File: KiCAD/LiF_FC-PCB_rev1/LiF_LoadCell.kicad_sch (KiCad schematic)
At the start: 29 parts, among them J17 LC 5V0_{EN}, J18 LC 3V3_{EN}, J19 Load Cell, U8 MCP6N11-xxxE/SN, U9 NCV8114ASN165T1G

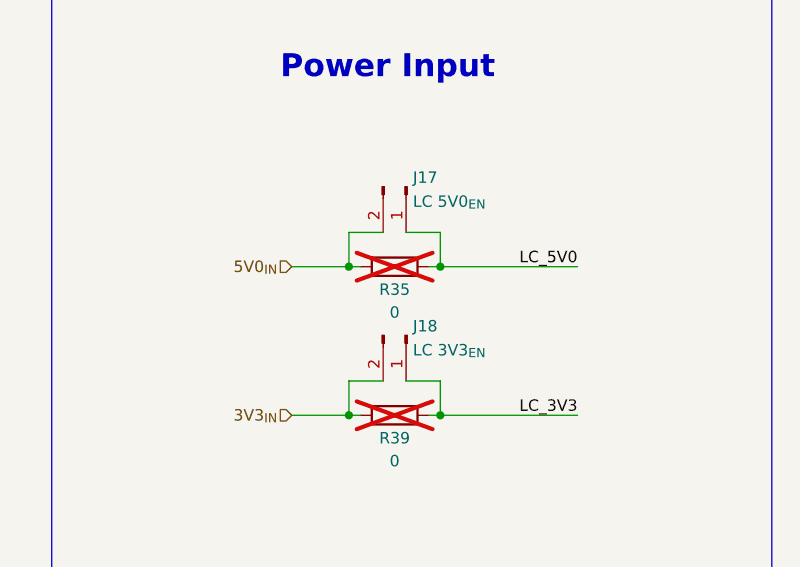
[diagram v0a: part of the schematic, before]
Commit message: Created new KiCAD project for IO PCB, moved relevant components there, saving backup before reannotating the Service PCB schematics
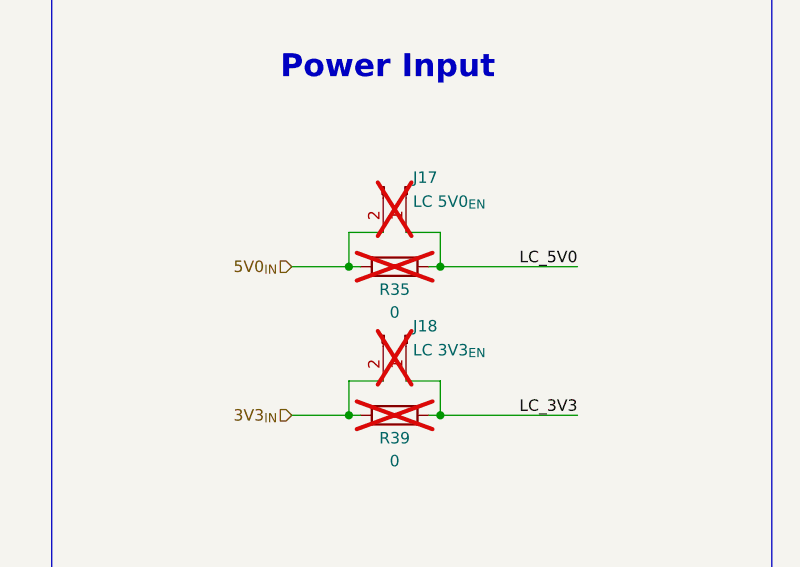
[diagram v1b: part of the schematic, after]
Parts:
- J17, J18: now not fitted; now left out of the parts list

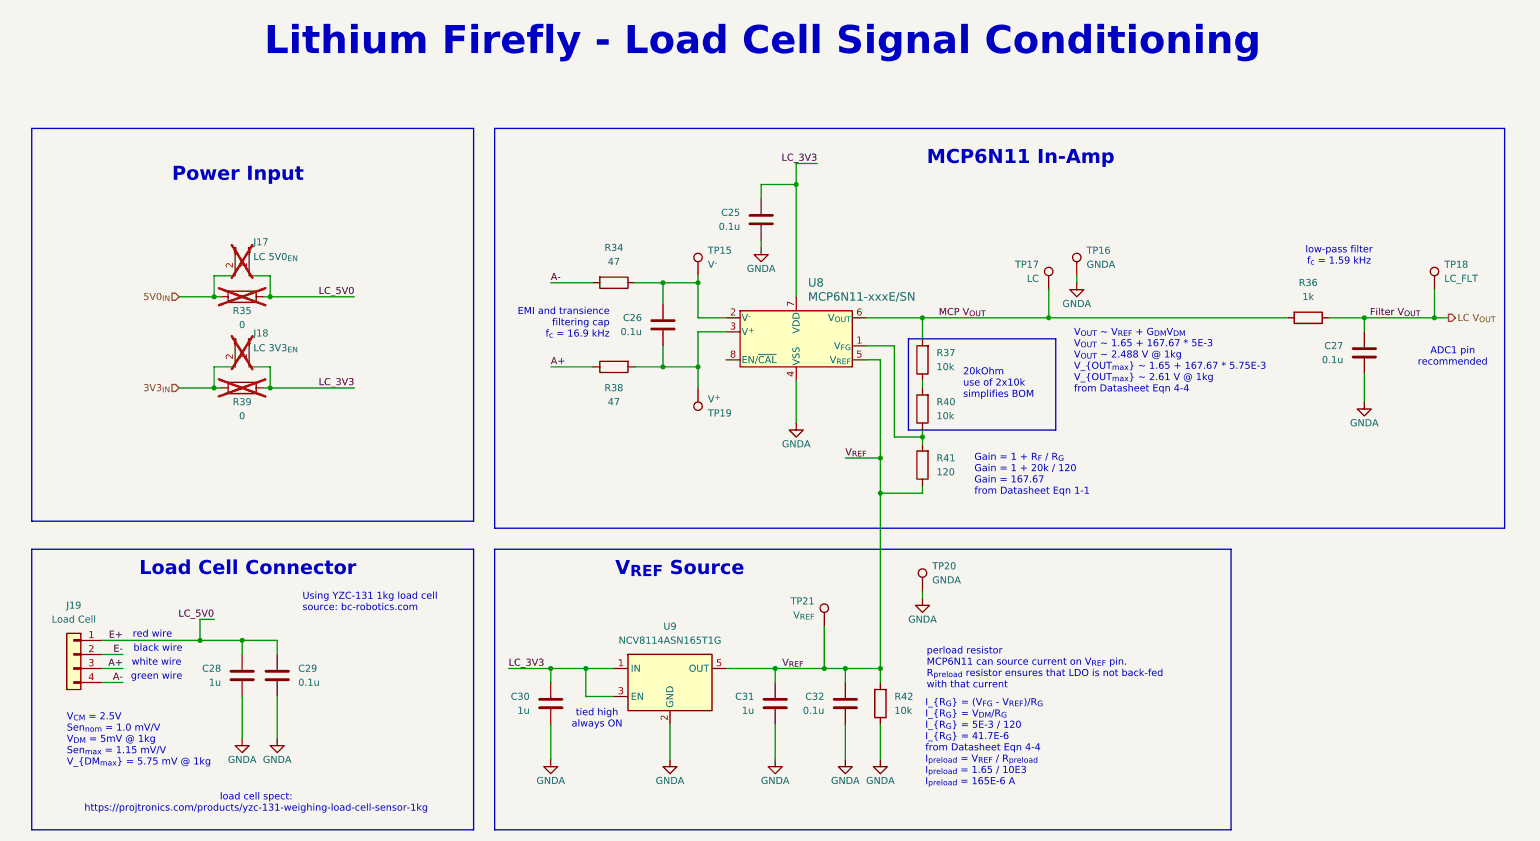
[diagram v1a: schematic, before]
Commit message: progress save for the night. landmarking of service PCB is almost done. redid the analog section layout to make it more assembleable and better utilze the space. Still need to do ACC, R3V3, IO, test points, and jumpers
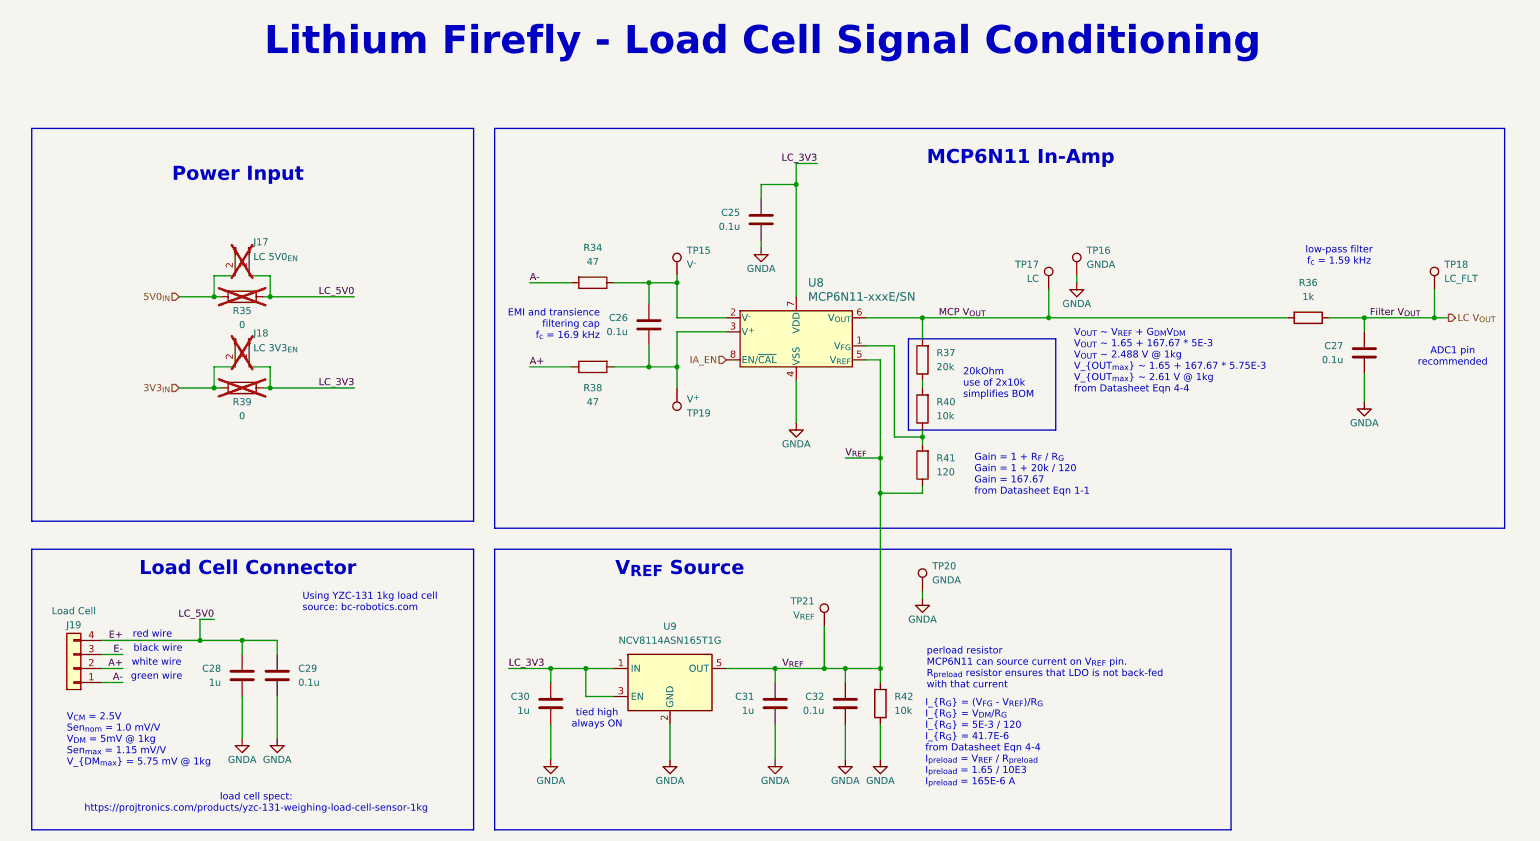
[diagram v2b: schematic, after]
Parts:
- R37: value 10k -> 20k
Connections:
- net A+: now also J19.2 (Pin_2); no longer J19.3 (Pin_3)
- net A-: now also J19.1 (Pin_1); no longer J19.4 (Pin_4)
- net E+: now also J19.4 (Pin_4); no longer J19.1 (Pin_1)
- net E-: now also J19.3 (Pin_3); no longer J19.2 (Pin_2)
- net IA_EN: now reaches U8.8 (EN/~{CAL})
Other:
- moved on the sheet: C26, J19, R34, R38, TP15, TP19

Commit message: routing backup
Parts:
- R39: now left out of the parts list
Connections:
- net LC_3V3 is gone; now on net 3V3_{IN}: C25.1, C30.1, J18.1 (Pin_1), R39.1, U8.7 (VDD), U9.1 (IN), U9.3 (EN)
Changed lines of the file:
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@@
+	)
+	(junction
+		(at 62.23 82.55)
+		(diameter 0)
+		(color 0 0 0 0)
 	)
 	(junction
@@
 	)
 	(junction
+		(at 44.45 82.55)
+		(diameter 0)
+		(color 0 0 0 0)
+	)
+	(junction
 		(at 132.08 78.74)
 		(diameter 0)
@@
 	(wire
 		(pts
+			(xy 62.23 82.55) (xy 73.66 82.55)
+		)
+		(stroke
+			(width 0)
+			(type default)
+		)
+	)
+	(wire
+		(pts
 			(xy 127 78.74) (xy 132.08 78.74)
 		)
@@
 	(wire
 		(pts
-			(xy 41.91 82.55) (xy 48.26 82.55)
+			(xy 41.91 82.55) (xy 44.45 82.55)
 		)
 		(stroke
@@
 	(wire
 		(pts
+			(xy 44.45 90.17) (xy 44.45 82.55)
+		)
+		(stroke
+			(width 0)
+			(type default)
+		)
+	)
+	(wire
+		(pts
 			(xy 45.72 124.46) (xy 45.72 128.27)
 		)
@@
 	(wire
 		(pts
+			(xy 44.45 82.55) (xy 48.26 82.55)
+		)
+		(stroke
+			(width 0)
+			(type default)
+		)
+	)
+	(wire
+		(pts
 			(xy 162.56 133.35) (xy 168.91 133.35)
 		)
@@
 	(wire
 		(pts
-			(xy 58.42 82.55) (xy 73.66 82.55)
+			(xy 58.42 82.55) (xy 62.23 82.55)
 		)
 		(stroke
@@
 	(wire
 		(pts
+			(xy 62.23 90.17) (xy 44.45 90.17)
+		)
+		(stroke
+			(width 0)
+			(type default)
+		)
+	)
+	(wire
+		(pts
 			(xy 120.65 63.5) (xy 127 63.5)
 		)
@@
 		(pts
 			(xy 256.54 80.01) (xy 256.54 85.09)
+		)
+		(stroke
+			(width 0)
+			(type default)
+		)
+	)
+	(wire
+		(pts
+			(xy 62.23 82.55) (xy 62.23 90.17)
 		)
 		(stroke
@@
 		(unit 1)
 		(exclude_from_sim no)
-		(in_bom yes)
-		(on_board yes)
+		(in_bom no)
+		(on_board no)
 		(dnp yes)
 		(property "Reference" "R39"

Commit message: finished service PCB routing and silkscreen, finished IO PCB layout, routing, and silkscreen. Exported production files, submitted PCB for manufacturing by JLCPCB
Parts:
- removed TP20: GNDA, TestPoint:TestPoint_Loop_D1.80mm_Drill1.0mm_Beaded, symbol Connector:TestPoint
- R34, R36, R37, R38, R40, R41, R42: footprint Capacitor_SMD:C_0805_2012Metric -> Resistor_SMD:R_0805_2012Metric
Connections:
- net E- is gone; now on net GNDA: J19.3 (Pin_3)
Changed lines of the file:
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@@
 	(wire
 		(pts
-			(xy 27.94 130.81) (xy 31.75 130.81)
+			(xy 27.94 130.81) (xy 44.45 130.81)
 		)
 		(stroke
@@
 	(wire
 		(pts
-			(xy 176.53 119.38) (xy 176.53 120.65)
+			(xy 44.45 139.7) (xy 44.45 130.81)
 		)
 		(stroke
@@
 	)
 	(symbol
-		(lib_id "power:GNDA")
-		(at 176.53 120.65 0)
+		(lib_id "Connector:TestPoint")
+		(at 269.24 64.77 0)
 		(unit 1)
 		(exclude_from_sim no)
@@
 		(on_board yes)
 		(dnp no)
-		(property "Reference" "#PWR051"
-			(at 176.53 127 0)
+		(property "Reference" "TP18"
+			(at 271.018 60.198 0)
 			(effects
 				(font
 					(size 1.27 1.27)
 				)
-				(hide yes)
+				(justify left)
 			)
 		)
-		(property "Value" "GNDA"
-			(at 176.53 124.46 0)
+		(property "Value" "LC_FLT"
+			(at 271.018 62.738 0)
 			(effects
 				(font
 					(size 1.27 1.27)
 				)
+				(justify left)
 			)
 		)
-		(property "Footprint" ""
-			(at 176.53 120.65 0)
+		(property "Footprint" "TestPoint:TestPoint_Loop_D1.80mm_Drill1.0mm_Beaded"
+			(at 274.32 64.77 0)
 			(effects
 				(font
@@
 			)
 		)
-		(property "Datasheet" ""
-			(at 176.53 120.65 0)
+		(property "Datasheet" "~"
+			(at 274.32 64.77 0)
 			(effects
 				(font
@@
 			)
 		)
-		(property "Description" ""
-			(at 176.53 120.65 0)
+		(property "Description" "test point"
+			(at 269.24 64.77 0)
 			(effects
 				(font
@@
 			)
 		)
-		(pin "1"
-		)
-		(instances
-			(project "LiF_FC-PCB_rev1"
-				(path "/9e3e8da7-e506-46c9-90e5-307e4ad30d29/17577359-df8d-4d28-9071-787d31b1b6da"
-					(reference "#PWR051")
-					(unit 1)
-				)
-			)
-		)
-	)
-	(symbol
-		(lib_id "Connector:TestPoint")
-		(at 269.24 64.77 0)
-		(unit 1)
-		(exclude_from_sim no)
-		(in_bom yes)
-		(on_board yes)
-		(dnp no)
-		(property "Reference" "TP18"
-			(at 271.018 60.198 0)
+		(property "PN" "5002"
+			(at 269.24 64.77 0)
 			(effects
 				(font
 					(size 1.27 1.27)
 				)
-				(justify left)
+				(hide yes)
 			)
 		)
-		(property "Value" "LC_FLT"
-			(at 271.018 62.738 0)
+		(property "DKPN" "36-5002-ND"
+			(at 269.24 64.77 0)
 			(effects
 				(font
 					(size 1.27 1.27)
 				)
-				(justify left)
+				(hide yes)
 			)
 		)
-		(property "Footprint" "TestPoint:TestPoint_Loop_D1.80mm_Drill1.0mm_Beaded"
-			(at 274.32 64.77 0)
+		(property "CREATOR" ""
+			(at 269.24 64.77 0)
 			(effects
 				(font
@@
 			)
 		)
-		(property "Datasheet" "~"
-			(at 274.32 64.77 0)
+		(property "Check_prices" ""
+			(at 269.24 64.77 0)
 			(effects
 				(font
@@
 			)
 		)
-		(property "Description" "test point"
+		(property "Description_1" ""
 			(at 269.24 64.77 0)
 			(effects
@@
 			)
 		)
-		(property "PN" "5002"
+		(property "DigiKey_Part_Number" ""
 			(at 269.24 64.77 0)
 			(effects
@@
 			)
 		)
-		(property "DKPN" "36-5002-ND"
+		(property "Package" ""
 			(at 269.24 64.77 0)
 			(effects
@@
 			)
 		)
-		(property "CREATOR" ""
+		(property "SNAPEDA_PN" ""
 			(at 269.24 64.77 0)
 			(effects
@@
 			)
 		)
-		(property "Check_prices" ""
+		(property "SnapEDA_Link" ""
 			(at 269.24 64.77 0)
 			(effects
@@
 			)
 		)
-		(property "Description_1" ""
+		(property "VERIFIER" ""
 			(at 269.24 64.77 0)
 			(effects
@@
 			)
 		)
-		(property "DigiKey_Part_Number" ""
-			(at 269.24 64.77 0)
+		(pin "1"
+		)
+		(instances
+			(project "LiF_FC-PCB_rev1"
+				(path "/9e3e8da7-e506-46c9-90e5-307e4ad30d29/17577359-df8d-4d28-9071-787d31b1b6da"
+					(reference "TP18")
+					(unit 1)
+				)
+			)
+		)
+	)
+	(symbol
+		(lib_id "power:GNDA")
+		(at 44.45 139.7 0)
+		(unit 1)
+		(exclude_from_sim no)
+		(in_bom yes)
+		(on_board yes)
+		(dnp no)
+		(property "Reference" "#PWR02"
+			(at 44.45 146.05 0)
 			(effects
 				(font
@@
 			)
 		)
-		(property "Package" ""
-			(at 269.24 64.77 0)
+		(property "Value" "GNDA"
+			(at 44.45 143.51 0)
 			(effects
 				(font
 					(size 1.27 1.27)
 				)
-				(hide yes)
 			)
 		)
-		(property "SNAPEDA_PN" ""
-			(at 269.24 64.77 0)
+		(property "Footprint" ""
+			(at 44.45 139.7 0)
 			(effects
 				(font
@@
 			)
 		)
-		(property "SnapEDA_Link" ""
-			(at 269.24 64.77 0)
+		(property "Datasheet" ""
+			(at 44.45 139.7 0)
 			(effects
 				(font
@@
 			)
 		)
-		(property "VERIFIER" ""
-			(at 269.24 64.77 0)
+		(property "Description" ""
+			(at 44.45 139.7 0)
 			(effects
 				(font
@@
 			(project "LiF_FC-PCB_rev1"
 				(path "/9e3e8da7-e506-46c9-90e5-307e4ad30d29/17577359-df8d-4d28-9071-787d31b1b6da"
-					(reference "TP18")
+					(reference "#PWR02")
 					(unit 1)
 				)
@@
 	)
 	(symbol
-		(lib_id "Connector:TestPoint")
-		(at 176.53 119.38 0)
-		(unit 1)
-		(exclude_from_sim no)
-		(in_bom yes)
-		(on_board yes)
-		(dnp no)
-		(property "Reference" "TP20"
-			(at 178.308 114.808 0)
-			(effects
-				(font
-					(size 1.27 1.27)
-				)
-				(justify left)
-			)
-		)
-		(property "Value" "GNDA"
-			(at 178.308 117.348 0)
-			(effects
-				(font
-					(size 1.27 1.27)
-				)
-				(justify left)
-			)
-		)
-		(property "Footprint" "TestPoint:TestPoint_Loop_D1.80mm_Drill1.0mm_Beaded"
-			(at 181.61 119.38 0)
-			(effects
-				(font
-					(size 1.27 1.27)
-				)
-				(hide yes)
-			)
-		)
-		(property "Datasheet" "~"
-			(at 181.61 119.38 0)
-			(effects
-				(font
-					(size 1.27 1.27)
-				)
-				(hide yes)
-			)
-		)
-		(property "Description" "test point"
-			(at 176.53 119.38 0)
-			(effects
-				(font
-					(size 1.27 1.27)
-				)
-				(hide yes)
-			)
-		)
-		(property "PN" "5002"
-			(at 176.53 119.38 0)
-			(effects
-				(font
-					(size 1.27 1.27)
-				)
-				(hide yes)
-			)
-		)
-		(property "DKPN" "36-5002-ND"
-			(at 176.53 119.38 0)
-			(effects
-				(font
-					(size 1.27 1.27)
-				)
-				(hide yes)
-			)
-		)
-		(property "CREATOR" ""
-			(at 176.53 119.38 0)
-			(effects
-				(font
-					(size 1.27 1.27)
-				)
-				(hide yes)
-			)
-		)
-		(property "Check_prices" ""
-			(at 176.53 119.38 0)
-			(effects
-				(font
-					(size 1.27 1.27)
-				)
-				(hide yes)
-			)
-		)
-		(property "Description_1" ""
-			(at 176.53 119.38 0)
-			(effects
-				(font
-					(size 1.27 1.27)
-				)
-				(hide yes)
-			)
-		)
-		(property "DigiKey_Part_Number" ""
-			(at 176.53 119.38 0)
-			(effects
-				(font
-					(size 1.27 1.27)
-				)
-				(hide yes)
-			)
-		)
-		(property "Package" ""
-			(at 176.53 119.38 0)
-			(effects
-				(font
-					(size 1.27 1.27)
-				)
-				(hide yes)
-			)
-		)
-		(property "SNAPEDA_PN" ""
-			(at 176.53 119.38 0)
-			(effects
-				(font
-					(size 1.27 1.27)
-				)
-				(hide yes)
-			)
-		)
-		(property "SnapEDA_Link" ""
-			(at 176.53 119.38 0)
-			(effects
-				(font
-					(size 1.27 1.27)
-				)
-				(hide yes)
-			)
-		)
-		(property "VERIFIER" ""
-			(at 176.53 119.38 0)
-			(effects
-				(font
-					(size 1.27 1.27)
-				)
-				(hide yes)
-			)
-		)
-		(pin "1"
-		)
-		(instances
-			(project "LiF_FC-PCB_rev1"
-				(path "/9e3e8da7-e506-46c9-90e5-307e4ad30d29/17577359-df8d-4d28-9071-787d31b1b6da"
-					(reference "TP20")
-					(unit 1)
-				)
-			)
-		)
-	)
-	(symbol
 		(lib_id "Device:R")
 		(at 53.34 82.55 270)
@@
 			)
 		)
-		(property "Footprint" "Capacitor_SMD:C_0805_2012Metric"
+		(property "Footprint" "Resistor_SMD:R_0805_2012Metric"
 			(at 246.38 68.072 90)
 			(effects
@@
 			)
 		)
-		(property "Footprint" "Capacitor_SMD:C_0805_2012Metric"
+		(property "Footprint" "Resistor_SMD:R_0805_2012Metric"
 			(at 178.308 77.47 90)
 			(effects
@@
 			)
 		)
-		(property "Footprint" "Capacitor_SMD:C_0805_2012Metric"
+		(property "Footprint" "Resistor_SMD:R_0805_2012Metric"
 			(at 170.688 139.7 90)
 			(effects
@@
 			)
 		)
-		(property "Footprint" "Capacitor_SMD:C_0805_2012Metric"
+		(property "Footprint" "Resistor_SMD:R_0805_2012Metric"
 			(at 116.84 61.722 90)
 			(effects
@@
 			)
 		)
-		(property "Footprint" "Capacitor_SMD:C_0805_2012Metric"
+		(property "Footprint" "Resistor_SMD:R_0805_2012Metric"
 			(at 178.308 96.52 90)
 			(effects
@@
 			)
 		)
-		(property "Footprint" "Capacitor_SMD:C_0805_2012Metric"
+		(property "Footprint" "Resistor_SMD:R_0805_2012Metric"
 			(at 178.308 86.36 90)
 			(effects
@@
 			)
 		)
-		(property "Footprint" "Capacitor_SMD:C_0805_2012Metric"
+		(property "Footprint" "Resistor_SMD:R_0805_2012Metric"
 			(at 116.84 76.962 90)
 			(effects
